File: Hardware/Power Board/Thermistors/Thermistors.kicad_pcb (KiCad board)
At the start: 2 copper layers, 95 x 113.8 mm, 5 parts, among them J1 Conn_01x05_MountingPin

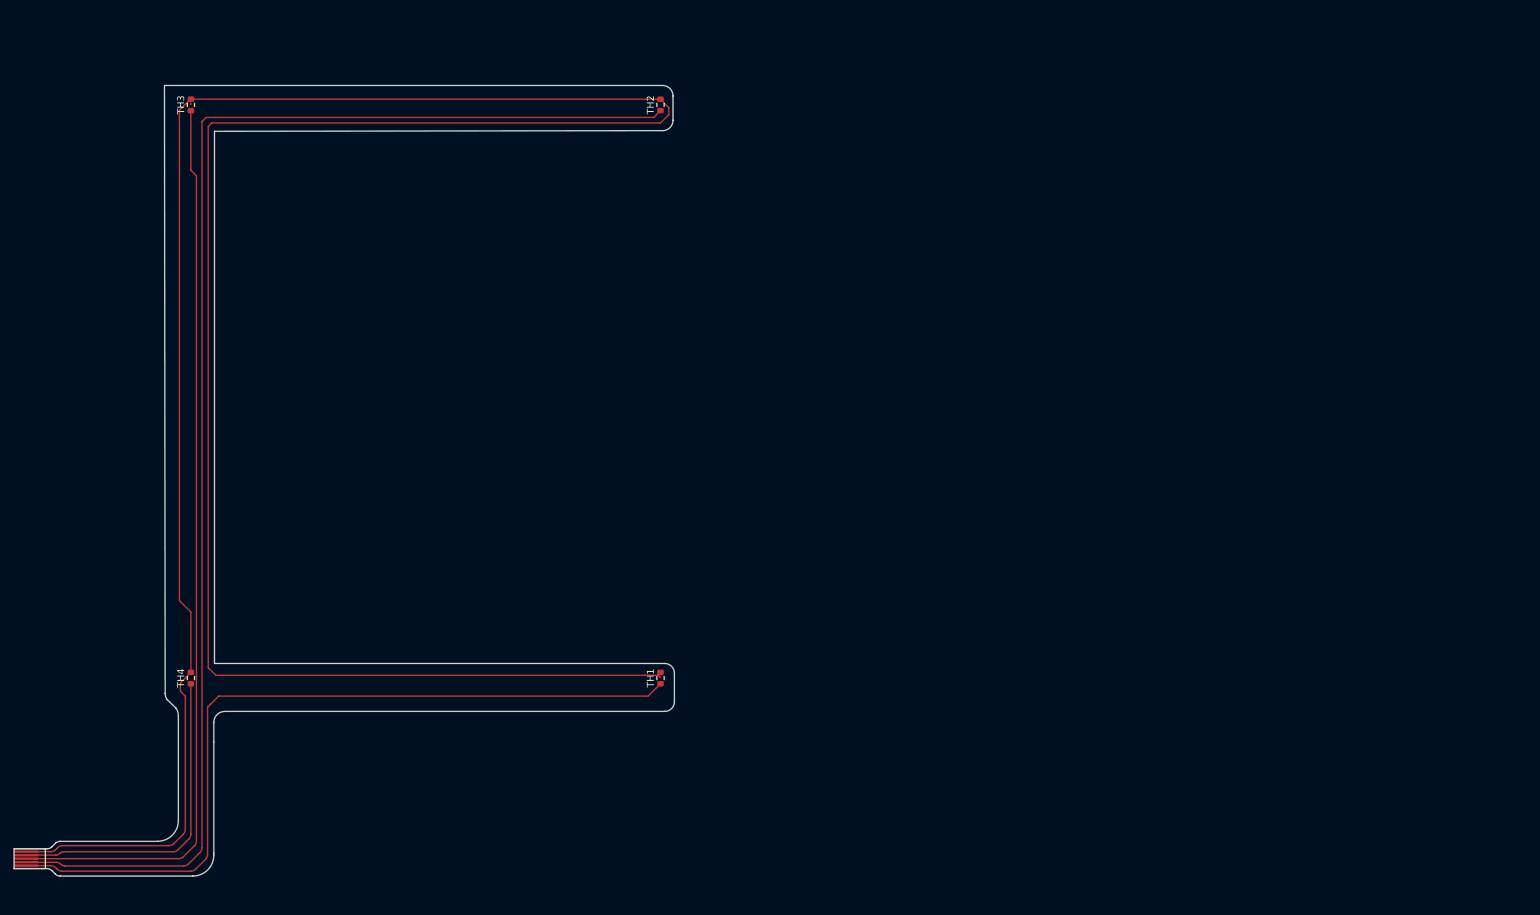
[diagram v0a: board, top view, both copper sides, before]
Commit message: update to some firmware stuff and updates/fab stuff for the thermsitor board
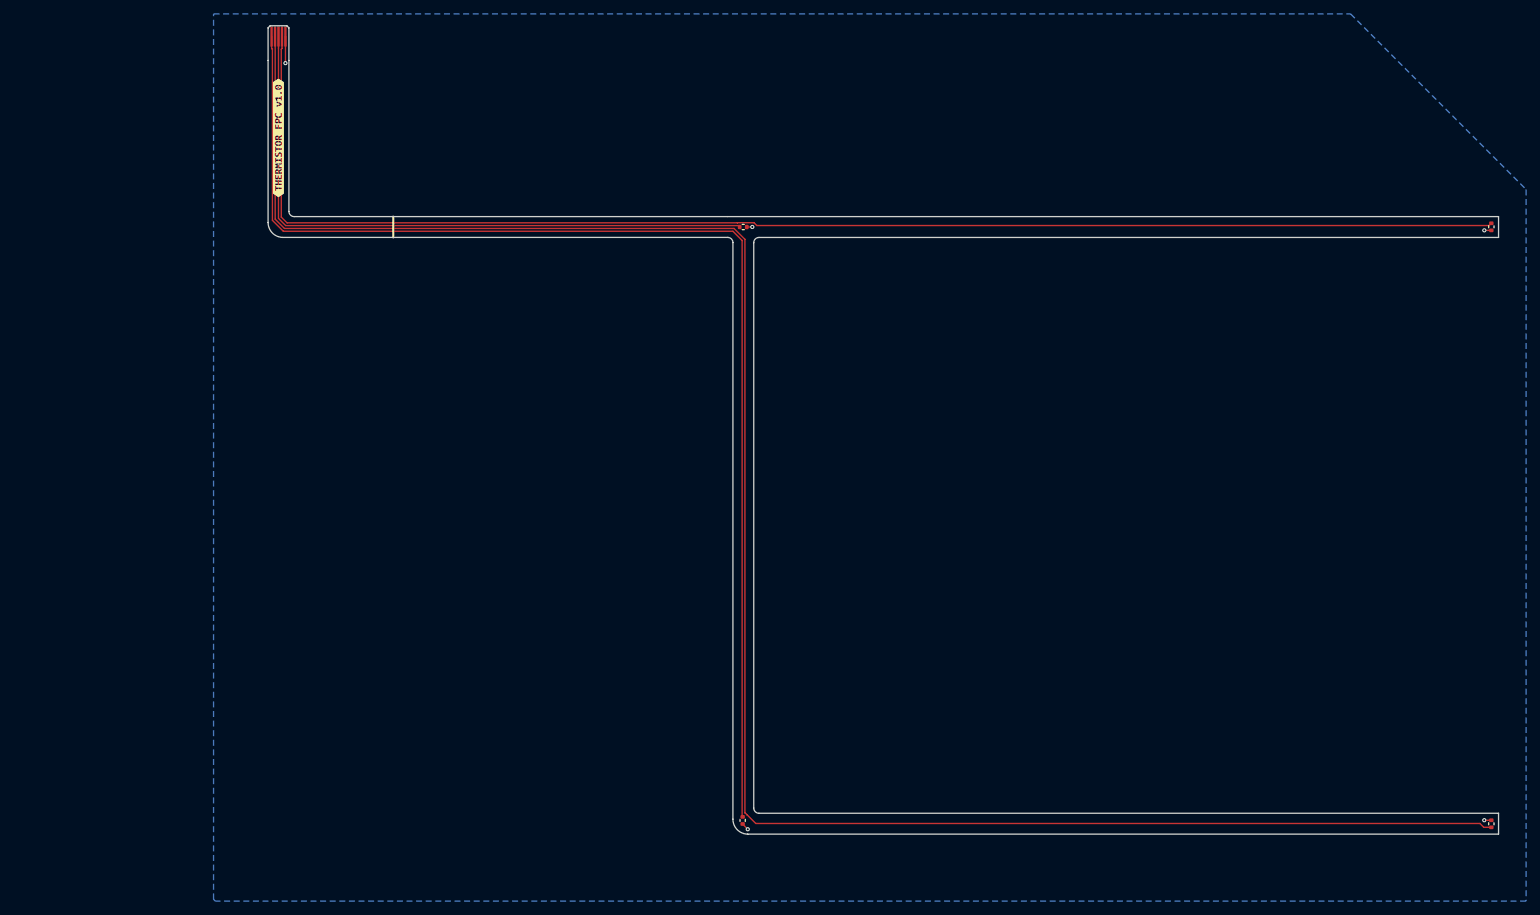
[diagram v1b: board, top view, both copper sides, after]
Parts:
- removed J1: Conn_01x05_MountingPin, Connector_TE-Connectivity:FPCB_TE_5_pin_Connector
- added J101: Conn_01x05, BAD_LIB:FPC_5pin, F.Cu at (72.2, 26.0)
- added kibuzzard-6936739F: G***, kibuzzard-6936739F, F.Cu at (72.2, 39.1)
- TH1, TH2: footprint Resistor_SMD:R_0603_1608Metric -> Resistor_SMD:R_0402_1005Metric
- TH3: renamed from TH4; footprint Resistor_SMD:R_0603_1608Metric -> Resistor_SMD:R_0402_1005Metric
- TH4: renamed from TH3; footprint Resistor_SMD:R_0603_1608Metric -> Resistor_SMD:R_0402_1005Metric
- moved TH4 188.0 mm to (246.8, 51.9), turned to -90 degrees
- moved TH2 158.1 mm to (246.8, 137.9)
- moved TH3 102.7 mm to (139.1, 52.0), turned to 0 degrees
- moved TH1 23.7 mm to (139.0, 137.4), turned to -90 degrees
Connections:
- TH3 pad 1: /TH_D -> /TH_C
- TH4 pad 1: /TH_C -> /TH_D
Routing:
- net GND: track 411.4 -> 9.18 mm, vias 0 -> 5
- net /TH_D: track 45.4 -> 200.9 mm
- net /TH_B: track 196.6 -> 286.0 mm
- net /TH_A: track 114.0 -> 178.4 mm
- net /TH_C: track 129.9 -> 93.1 mm
- added copper zone on B.Cu, net GND
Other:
- board size 95 x 113.8 mm -> 177.1 x 111.4 mm
- board text removed: "TH1"
